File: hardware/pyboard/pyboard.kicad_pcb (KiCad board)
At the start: 2 copper layers, 65 parts, among them J1 Battery, J2 Arduino_Mega2560_Shield, J6 USB_B_Micro, J9 Micro_SD_SCHA5B0200, Q1 IRLML6402, Q2 IRLML6402, SW1 RST, SW2 USR, U1 STM32F405RGT6, U2 MCP1703A-3302_SOT89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

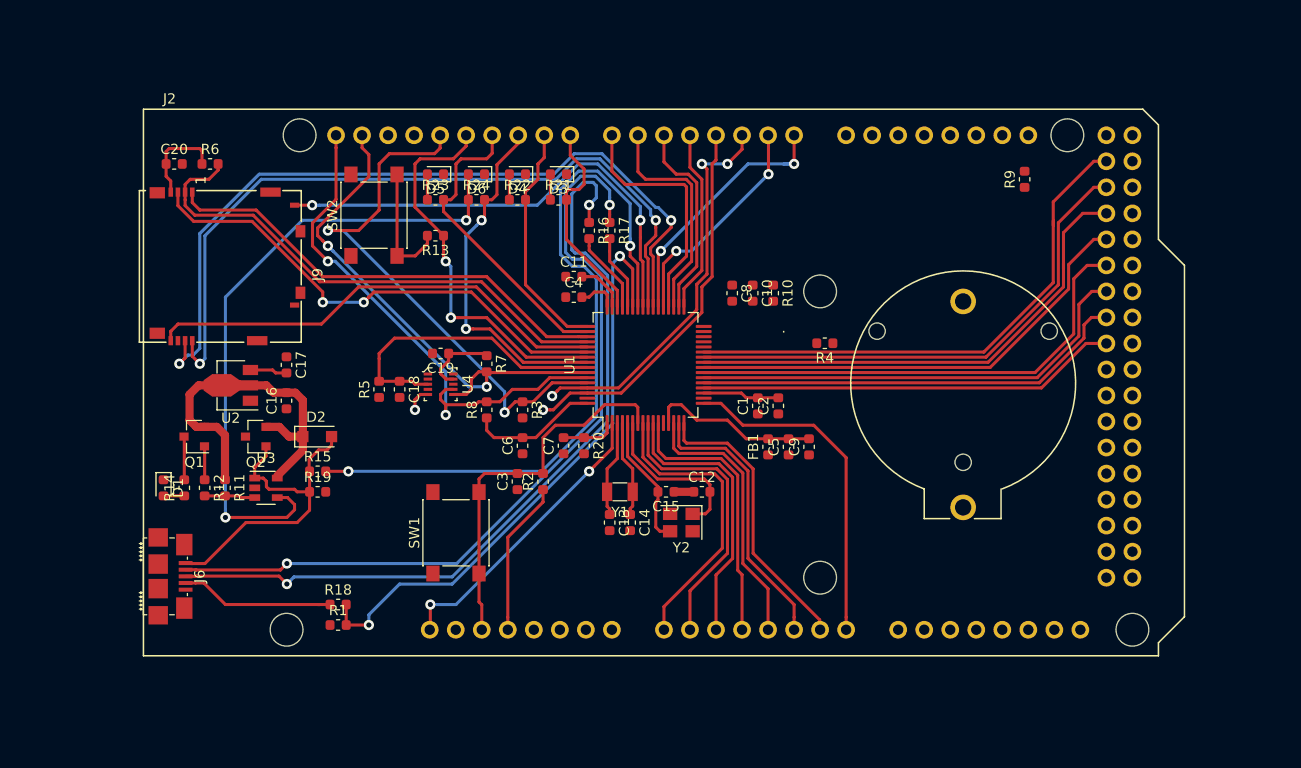
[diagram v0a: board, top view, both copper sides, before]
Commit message: Trace most of the components
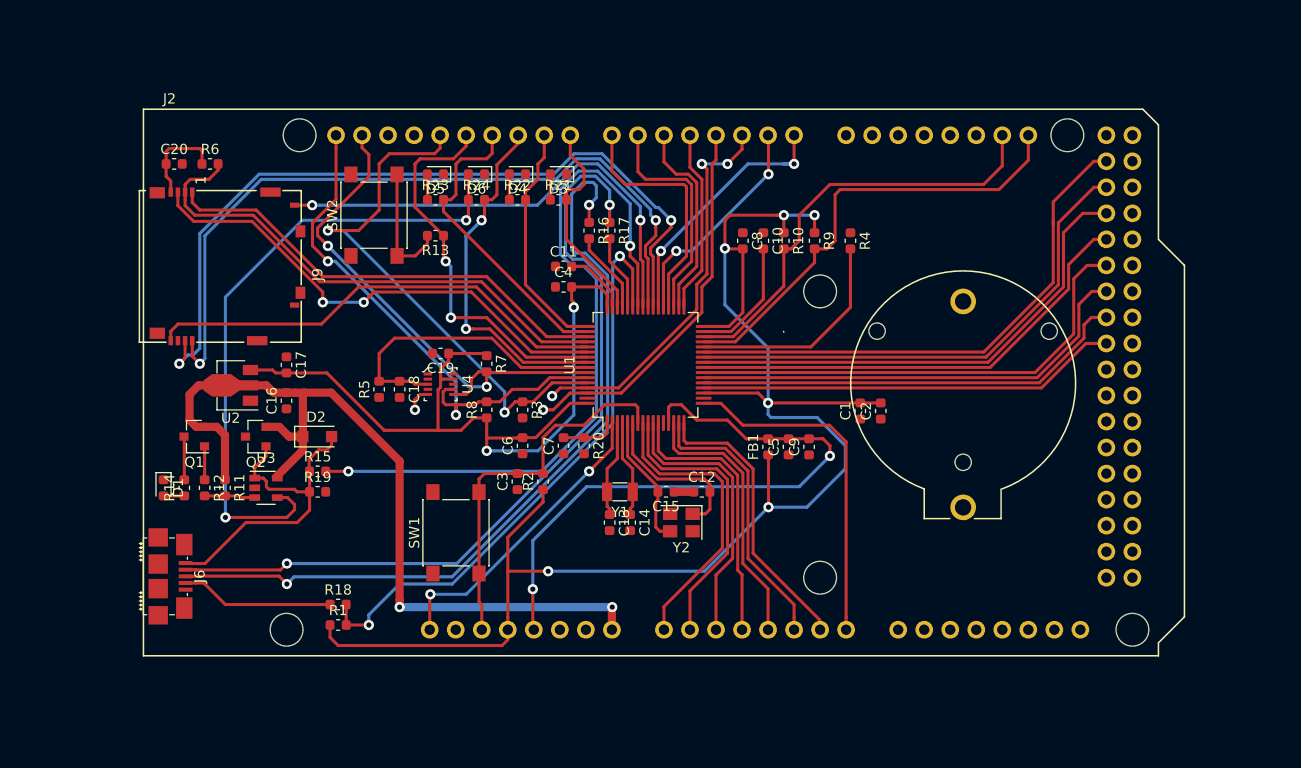
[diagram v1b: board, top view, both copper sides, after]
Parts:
- moved R9 21.4 mm to (165.5, 79.5), turned to 270 degrees
- moved R4 10.3 mm to (169.0, 79.5), turned to 270 degrees
- moved C1 10.0 mm to (170.0, 96.1)
- moved C2 10.0 mm to (172.0, 96.1)
- moved C10 5.21 mm to (160.5, 79.5)
- moved C8 5.21 mm to (158.5, 79.5)
- moved R10 5.21 mm to (162.5, 79.5)
- moved C11 1.41 mm to (141.0, 82.0)
- moved C4 1.41 mm to (141.0, 84.0)
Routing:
- net +3V3: track 59.6 -> 241.7 mm, vias 0 -> 8
- net VCC: track 31.4 -> 81.3 mm, vias 0 -> 2
- net /Y9: track 0.00 -> 44.9 mm
- net VDDA: track 16.7 -> 61.2 mm, vias 0 -> 2
- net /Y10: track 0.00 -> 42.6 mm
- net /BOOT1-MMA-INT: track 2.47 -> 24.1 mm
- net /VCAP_1: track 0.00 -> 12.1 mm
- net /VCAP_2: track 4.99 -> 6.41 mm
- net /X4: track 32.9 -> 33.8 mm
- net /X18: track 29.0 -> 29.6 mm

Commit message: Trace all components
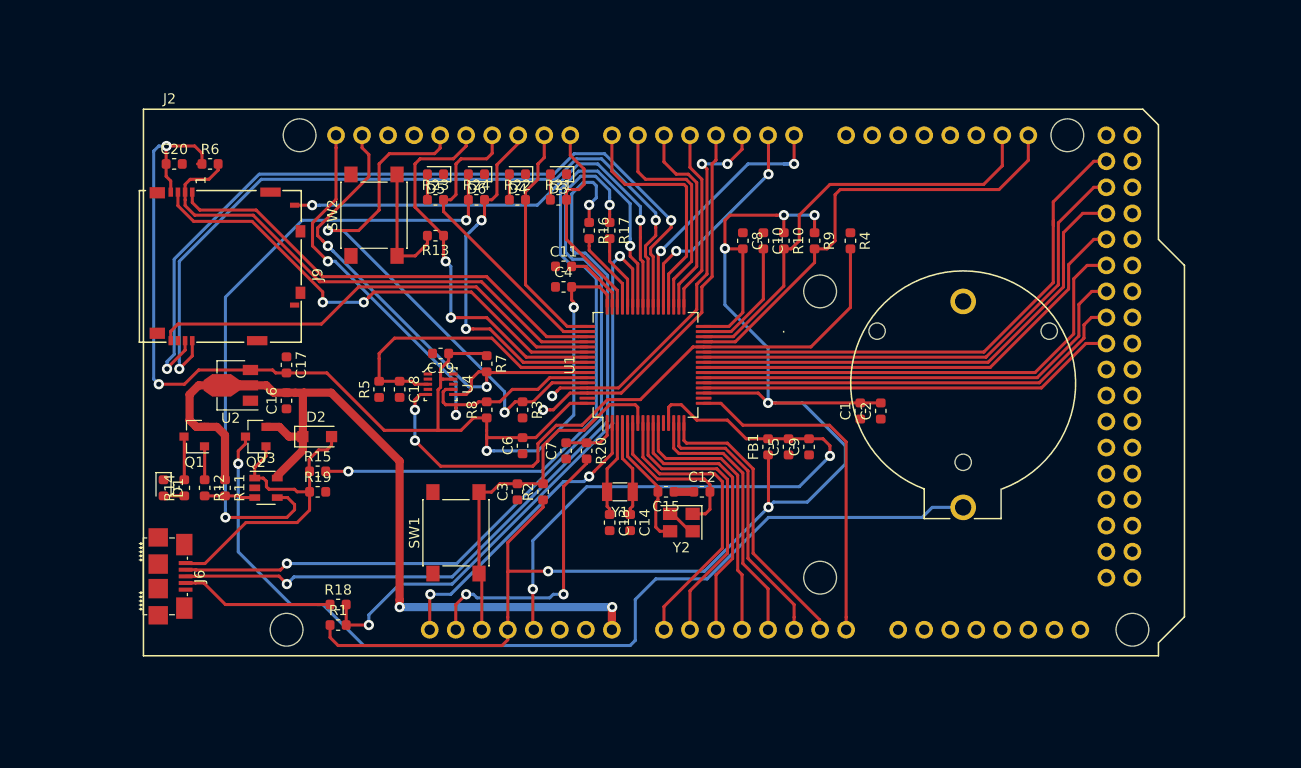
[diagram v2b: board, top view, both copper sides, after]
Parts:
- moved C3 1.00 mm to (136.5, 104.0)
- moved R2 1.00 mm to (139.0, 104.0)
- moved C7 0.56 mm to (141.2, 100.0)
- moved R20 0.56 mm to (143.2, 100.0)
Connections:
- J2 pad 5V3: VCC -> (no net)
- J2 pad 5V4: Net-(J2-Pad5V4) -> (no net)
- J2 pad IORF: (no net) -> Net-(J2-PadIORF)
- R20 pad 2: Net-(J2-Pad5V4) -> Net-(J2-PadIORF)
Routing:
- net Net-(J1-Pad1): track 0.00 -> 94.0 mm, vias 0 -> 1
- net /BOOT1-MMA-INT: track 24.1 -> 62.1 mm, vias 1 -> 2
- net +3V3: track 241.7 -> 274.2 mm, vias 8 -> 10
- net Net-(J2-PadIORF): track 0.00 -> 27.8 mm, vias 0 -> 2
- net VCC: track 81.3 -> 85.3 mm
- net GND: track 1.93 -> 5.08 mm
- net /SDIO_D1: track 74.1 -> 76.3 mm
- net /SDIO_D0: track 77.6 -> 79.4 mm
- net /~RST: track 37.0 -> 36.4 mm
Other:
- rule trace_min: 0.2 -> 0.3

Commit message: Add cooper polygon
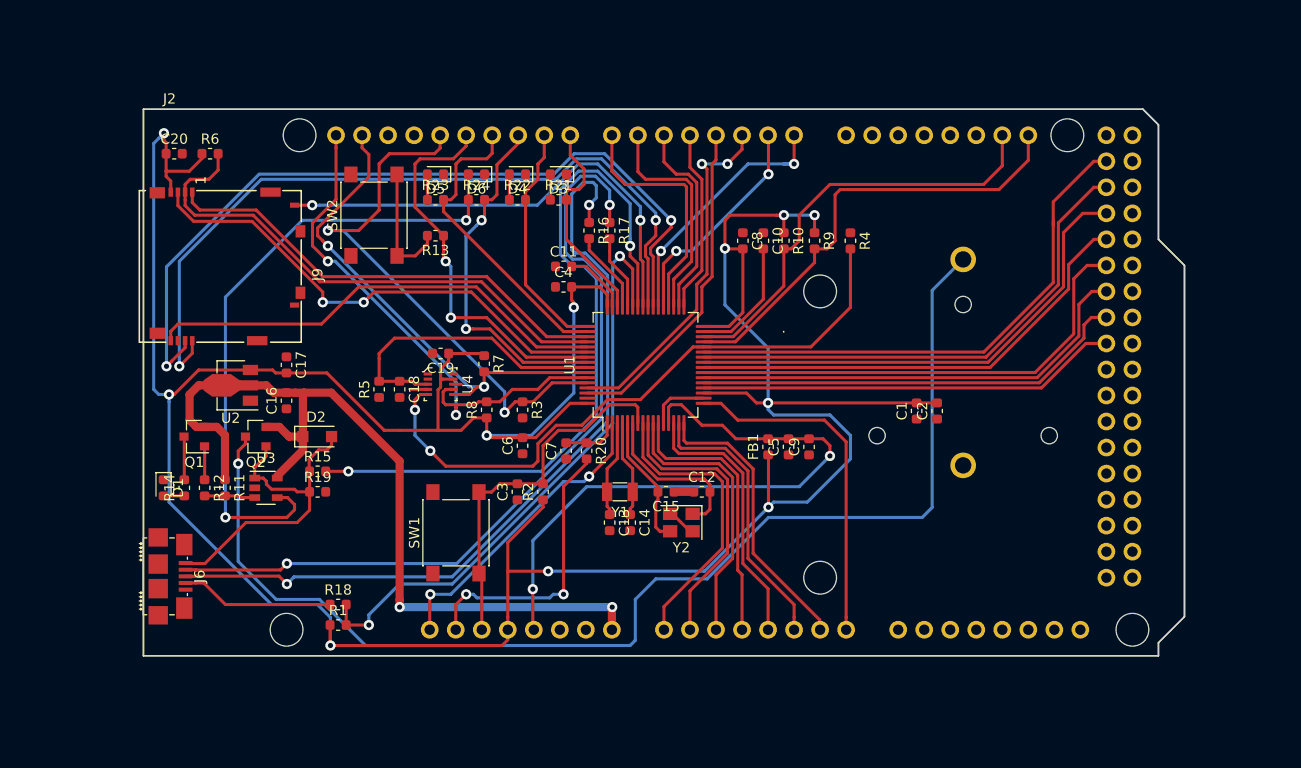
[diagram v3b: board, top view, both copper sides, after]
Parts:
- J1: moved to B.Cu
- moved C1 5.50 mm to (175.5, 96.1)
- moved C2 5.50 mm to (177.5, 96.1)
- moved C20 1.00 mm to (103.0, 71.0)
- moved R6 1.00 mm to (106.5, 71.0)
- moved R7 0.25 mm to (133.2, 91.5)
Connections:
- J6 pad CGND: (no net) -> GND
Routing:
- net +3V3: track 274.2 -> 314.9 mm, vias 10 -> 11
- net Net-(J1-Pad1): track 94.0 -> 117.0 mm
- net GND: track 5.08 -> 13.5 mm
- net /Y4: track 37.5 -> 32.5 mm, vias 1 -> 0
- net /Y3: track 38.3 -> 34.6 mm, vias 3 -> 2
- net /SCL: track 50.8 -> 49.5 mm
- net /SDIO_D3: track 51.2 -> 52.2 mm
- net /SDIO_D0: track 79.4 -> 78.8 mm
- net /SDIO_D1: track 76.3 -> 75.8 mm
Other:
- board outline added: 101.6 x 53.3 mm

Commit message: Trace all nets
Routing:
- net GND: track 13.5 -> 96.6 mm, vias 0 -> 9
- net /SDIO_D0: track 78.8 -> 77.3 mm
- net /SDIO_D1: track 75.8 -> 74.3 mm
- net /BLU: track 35.4 -> 33.9 mm
- net /B: track 62.7 -> 64.0 mm
- net /SW: track 38.1 -> 37.6 mm
- net +3V3: track 314.9 -> 315.5 mm
- added copper zone on B.Cu, net GND
- added copper zone on F.Cu, net GND
